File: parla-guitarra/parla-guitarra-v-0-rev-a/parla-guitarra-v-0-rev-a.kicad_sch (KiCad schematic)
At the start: 10 parts, among them J1 AudioJack2_SwitchT, J2 Screw_Terminal_01x02, U1 LM386

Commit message: agregar borde pcb
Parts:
- U1: footprint (none) -> Package_DIP:DIP-8_W7.62mm_Socket_LongPads
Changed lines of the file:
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@@
 			)
 		)
-		(property "Footprint" ""
+		(property "Footprint" "Package_DIP:DIP-8_W7.62mm_Socket_LongPads"
 			(at 110.49 59.69 0)
 			(hide yes)

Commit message: agregar terminal block
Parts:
- J2, LS1: footprint (none) -> TerminalBlock:TerminalBlock_MaiXu_MX126-5.0-02P_1x02_P5.00mm
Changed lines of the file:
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@@
 			)
 		)
-		(property "Footprint" ""
+		(property "Footprint" "TerminalBlock:TerminalBlock_MaiXu_MX126-5.0-02P_1x02_P5.00mm"
 			(at 27.94 33.02 0)
 			(hide yes)
@@
 			)
 		)
-		(property "Footprint" ""
+		(property "Footprint" "TerminalBlock:TerminalBlock_MaiXu_MX126-5.0-02P_1x02_P5.00mm"
 			(at 152.4 67.31 0)
 			(hide yes)

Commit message: agregar mas apuntes
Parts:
- added D1: D, symbol Device:D
- added U2: TL072, symbol Amplifier_Operational:TL072
- J1: value AudioJack2_SwitchT -> entrada
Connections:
- net +9V: now also D1.1 (K); no longer J2.1 (Pin_1)
- new net: D1.2 (A), J2.1 (Pin_1)
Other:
- note added: "alimentacion 9v"
- note added: "diodo de proteccion condensadores estabilizacion"
- moved on the sheet: J1

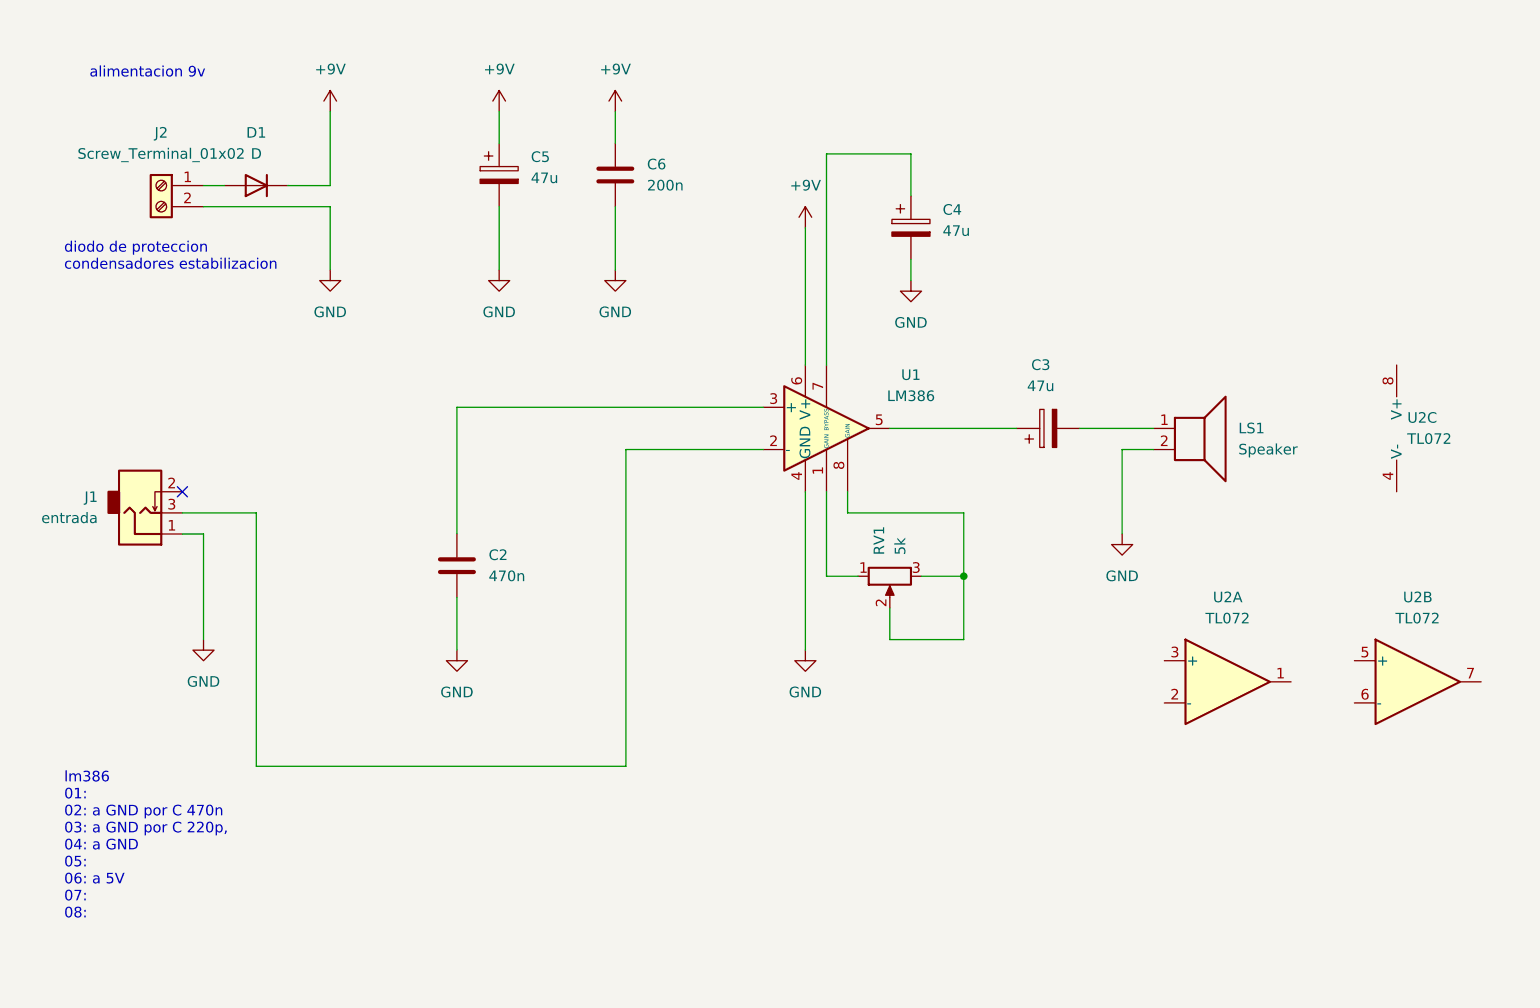
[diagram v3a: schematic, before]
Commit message: agregar parla-guitarra borrador
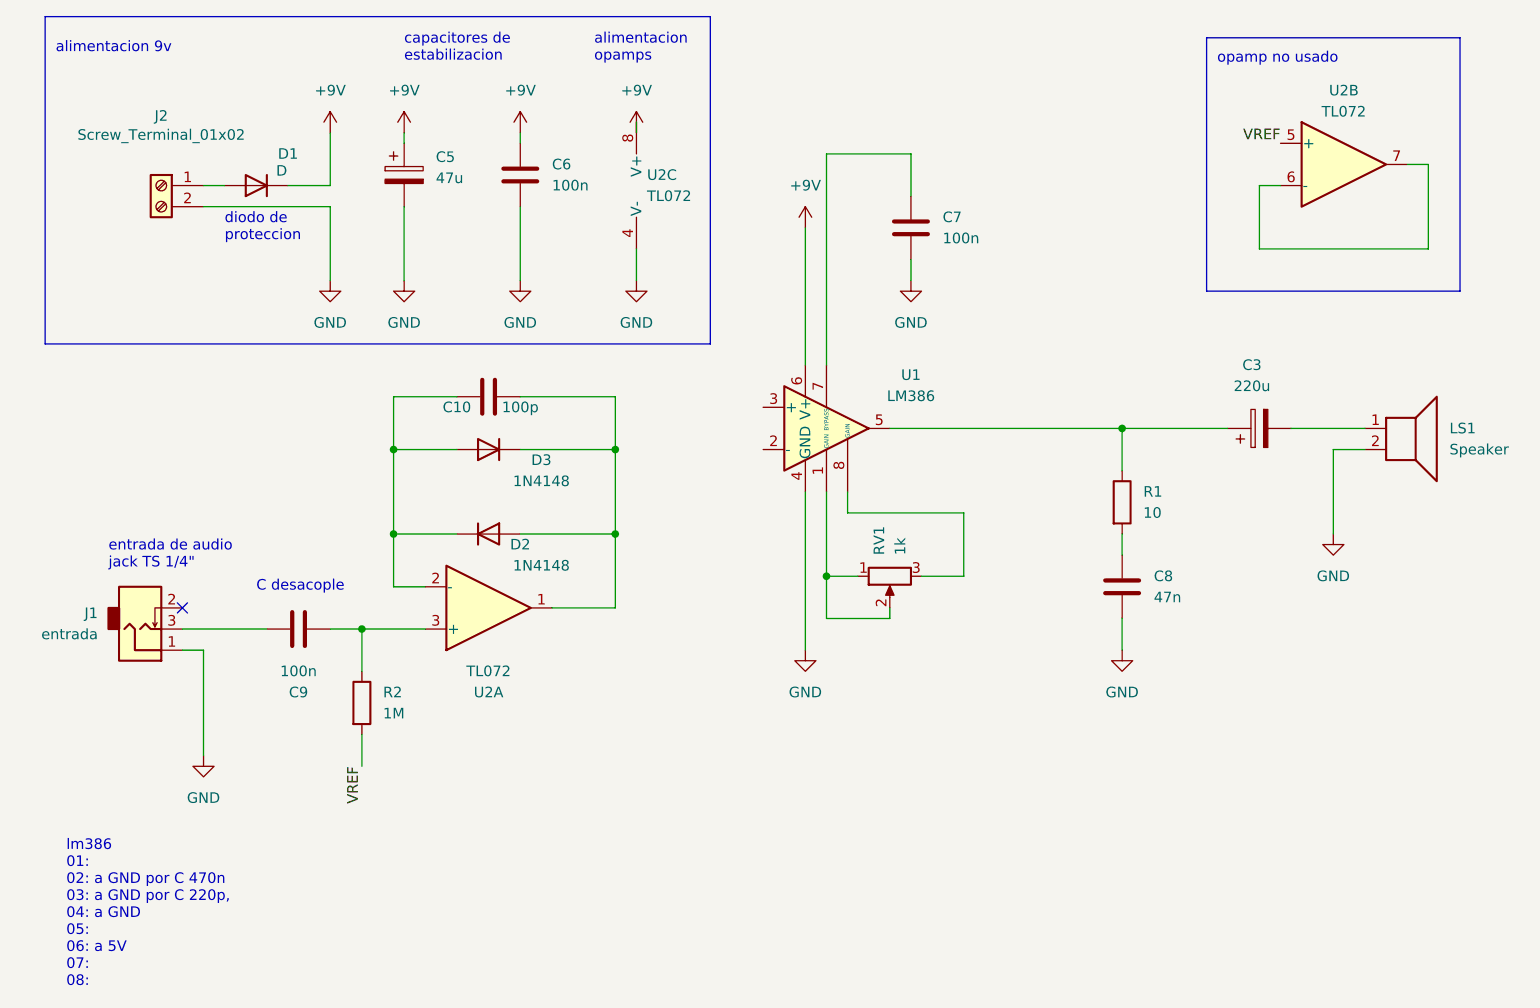
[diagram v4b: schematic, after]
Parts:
- removed C2: 470n, symbol Device:C
- removed C4: 47u, symbol Device:C_Polarized
- added C10: 100p, symbol Device:C
- added C7, C9: 100n, symbol Device:C
- added C8: 47n, symbol Device:C
- added D2, D3: 1N4148, Diode_THT:D_DO-35_SOD27_P7.62mm_Horizontal, symbol Diode:1N4148
- added R1: 10, symbol Device:R
- added R2: 1M, symbol Device:R
- C3: value 47u -> 220u
- C6: value 200n -> 100n
- RV1: value 5k -> 1k
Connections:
- net +9V: now also U2.8 (V+)
- net GND: now also U2.4 (V-), C7.2, C8.2
- net at J1.3: now also C9.1; no longer U1.2 (-)
- net at U2.1: now also C10.2, D2.2 (A), D3.1 (K)
- net at U2.2 (-): now also C10.1, D2.1 (K), D3.2 (A)
- net at U2.3 (+): now also C9.2, R2.1
- net at RV1.1, U1.1 (GAIN): now also RV1.2
- net at RV1.3, U1.8 (GAIN): no longer RV1.2
- net at C3.1, U1.5: now also R1.1
- net at U1.7 (BYPASS): now also C7.1
- net VREF: now reaches U2.5 (+)
- net VREF: now also R2.2
- net at U2.6 (-): now also U2.7
- new net: C8.1, R1.2
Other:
- note added: "C desacople"
- note added: "alimentacion opamps"
- note added: "capacitores de estabilizacion"
- note added: "diodo de proteccion"
- note added: "entrada de audio jack TS 1/4""
- note added: "opamp no usado"
- note removed: "diodo de proteccion condensadores estabilizacion"
- title: parla-guitarra -> parla-guitarra-v-0
- moved on the sheet: C5, C6, J1
